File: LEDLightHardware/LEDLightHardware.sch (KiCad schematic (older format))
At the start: 1 part

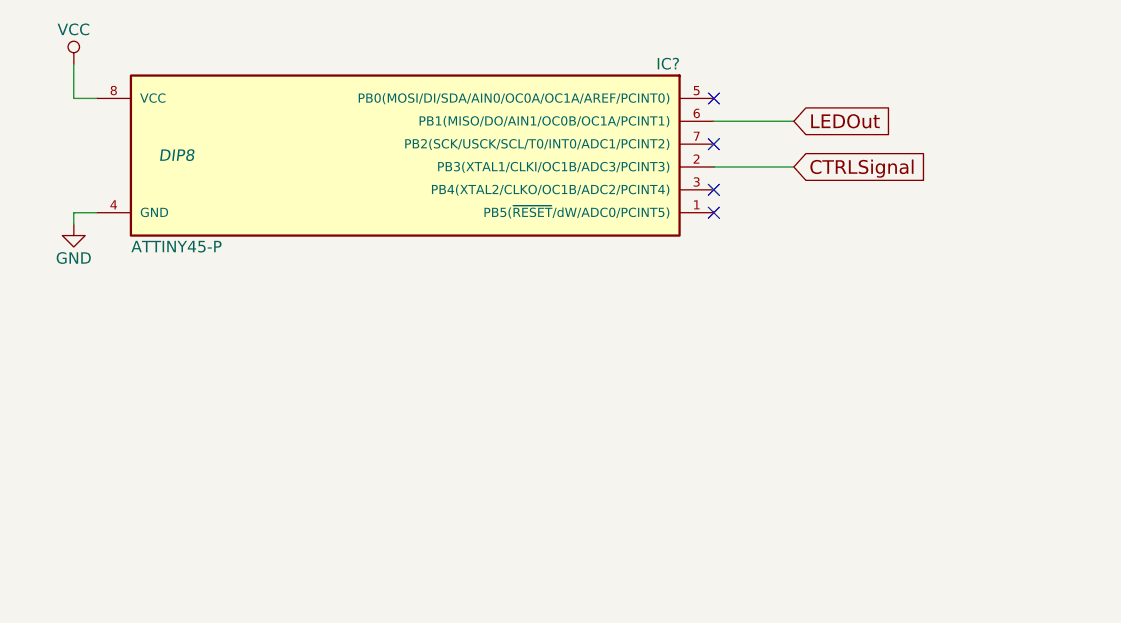
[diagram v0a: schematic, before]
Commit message: Added power input and regulation
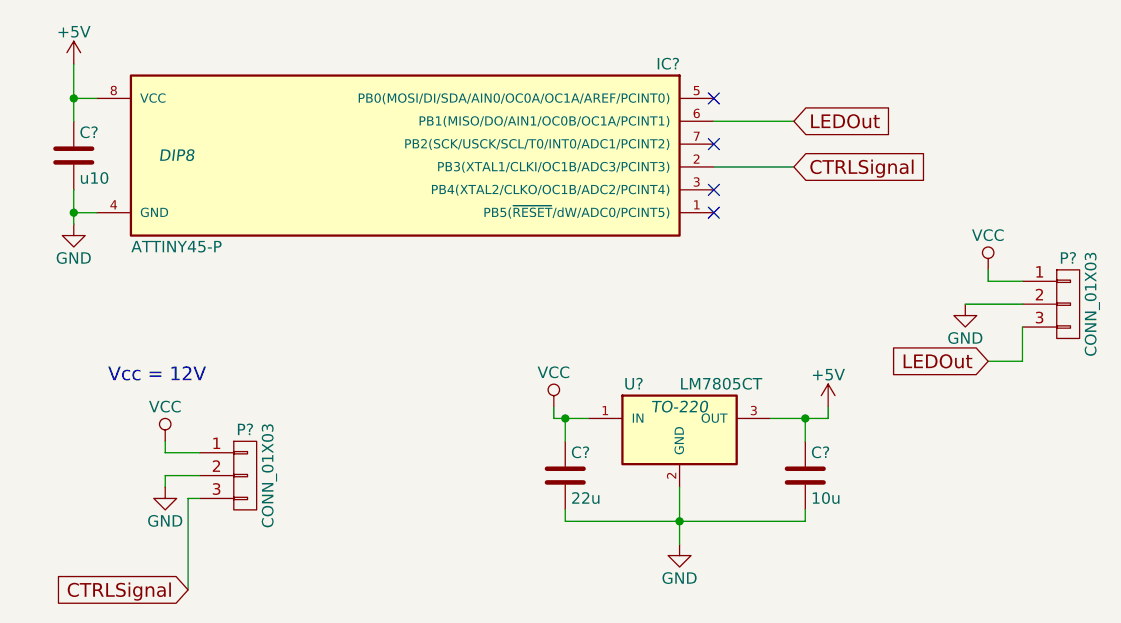
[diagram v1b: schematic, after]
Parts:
- added C?: u10, symbol C
- added C?: 22u, symbol C
- added C?: 10u, symbol C
- added P? (x2): CONN_01X03, symbol CONN_01X03
- added U?: LM7805CT, TO-220, symbol LM7805CT
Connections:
- net CTRLSignal: now also P?.3 (P3)
- net GND: now also C?.2, C?.2, C?.2, P?.2 (P2), P?.2 (P2), U?.2 (GND)
- net LEDOut: now also P?.3 (P3)
- net VCC: now also C?.1, P?.1 (P1), P?.1 (P1), U?.1 (IN); no longer IC?.8 (VCC)
- new net +5V: C?.1, C?.1, IC?.8 (VCC), U?.3 (OUT)
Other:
- note added: "Vcc = 12V"
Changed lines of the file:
@@
 	-1   0    0    -1
 $EndComp
-$Comp
-L VCC #PWR?
-U 1 1 56FFFF56
-P 1250 1050
-F 0 "#PWR?" H 1250 900 50  0001 C CNN
-F 1 "VCC" H 1250 1200 50  0000 C CNN
-F 2 "" H 1250 1050 50  0000 C CNN
-F 3 "" H 1250 1050 50  0000 C CNN
-	1    1250 1050
-	1    0    0    -1
-$EndComp
-Wire Wire Line
-	1250 1050 1250 1200
+Wire Wire Line
+	1250 1050 1250 1300
 Wire Wire Line
 	1250 1200 1350 1200
@@
 $EndComp
 Wire Wire Line
-	1250 1750 1250 1700
+	1250 1600 1250 1750
 Wire Wire Line
 	1250 1700 1350 1700
@@
 NoConn ~ 4050 1700
 NoConn ~ 4050 1600
+$Comp
+L VCC #PWR?
+U 1 1 57012428
+P 1650 2700
+F 0 "#PWR?" H 1650 2550 50  0001 C CNN
+F 1 "VCC" H 1650 2850 50  0000 C CNN
+F 2 "" H 1650 2700 50  0000 C CNN
+F 3 "" H 1650 2700 50  0000 C CNN
+	1    1650 2700
+	1    0    0    -1
+$EndComp
+Wire Wire Line
+	1650 2700 1650 2750
+Wire Wire Line
+	1650 2750 1800 2750
+$Comp
+L GND #PWR?
+U 1 1 5701244A
+P 1650 2900
+F 0 "#PWR?" H 1650 2650 50  0001 C CNN
+F 1 "GND" H 1650 2750 50  0000 C CNN
+F 2 "" H 1650 2900 50  0000 C CNN
+F 3 "" H 1650 2900 50  0000 C CNN
+	1    1650 2900
+	1    0    0    -1
+$EndComp
+Wire Wire Line
+	1650 2900 1650 2850
+Wire Wire Line
+	1650 2850 1800 2850
+$Comp
+L C C?
+U 1 1 570124BC
+P 1250 1450
+F 0 "C?" H 1275 1550 50  0000 L CNN
+F 1 "u10" H 1275 1350 50  0000 L CNN
+F 2 "" H 1288 1300 50  0000 C CNN
+F 3 "" H 1250 1450 50  0000 C CNN
+	1    1250 1450
+	1    0    0    -1
+$EndComp
+Connection ~ 1250 1200
+Connection ~ 1250 1700
+Text Notes 1400 2450 0    60   ~ 0
+Vcc = 12V
+$Comp
+L LM7805CT U?
+U 1 1 57012653
+P 3900 2650
+F 0 "U?" H 3700 2850 50  0000 C CNN
+F 1 "LM7805CT" H 3900 2850 50  0000 L CNN
+F 2 "TO-220" H 3900 2750 50  0000 C CIN
+F 3 "" H 3900 2650 50  0000 C CNN
+	1    3900 2650
+	1    0    0    -1
+$EndComp
+$Comp
+L VCC #PWR?
+U 1 1 570126D6
+P 3350 2550
+F 0 "#PWR?" H 3350 2400 50  0001 C CNN
+F 1 "VCC" H 3350 2700 50  0000 C CNN
+F 2 "" H 3350 2550 50  0000 C CNN
+F 3 "" H 3350 2550 50  0000 C CNN
+	1    3350 2550
+	1    0    0    -1
+$EndComp
+Wire Wire Line
+	3350 2550 3350 2600
+Wire Wire Line
+	3350 2600 3500 2600
+Wire Wire Line
+	3900 2900 3900 3150
+$Comp
+L +5V #PWR?
+U 1 1 57012788
+P 4550 2550
+F 0 "#PWR?" H 4550 2400 50  0001 C CNN
+F 1 "+5V" H 4550 2690 50  0000 C CNN
+F 2 "" H 4550 2550 50  0000 C CNN
+F 3 "" H 4550 2550 50  0000 C CNN
+	1    4550 2550
+	1    0    0    -1
+$EndComp
+Wire Wire Line
+	4550 2550 4550 2600
+Wire Wire Line
+	4550 2600 4300 2600
+$Comp
+L +5V #PWR?
+U 1 1 5701281E
+P 1250 1050
+F 0 "#PWR?" H 1250 900 50  0001 C CNN
+F 1 "+5V" H 1250 1190 50  0000 C CNN
+F 2 "" H 1250 1050 50  0000 C CNN
+F 3 "" H 1250 1050 50  0000 C CNN
+	1    1250 1050
+	1    0    0    -1
+$EndComp
+$Comp
+L C C?
+U 1 1 570129AF
+P 3400 2850
+F 0 "C?" H 3425 2950 50  0000 L CNN
+F 1 "22u" H 3425 2750 50  0000 L CNN
+F 2 "" H 3438 2700 50  0000 C CNN
+F 3 "" H 3400 2850 50  0000 C CNN
+	1    3400 2850
+	1    0    0    -1
+$EndComp
+Wire Wire Line
+	3400 3000 3400 3050
+Wire Wire Line
+	3400 3050 4450 3050
+$Comp
+L GND #PWR?
+U 1 1 57012A19
+P 3900 3150
+F 0 "#PWR?" H 3900 2900 50  0001 C CNN
+F 1 "GND" H 3900 3000 50  0000 C CNN
+F 2 "" H 3900 3150 50  0000 C CNN
+F 3 "" H 3900 3150 50  0000 C CNN
+	1    3900 3150
+	1    0    0    -1
+$EndComp
+Connection ~ 3900 3050
+$Comp
+L C C?
+U 1 1 57012A54
+P 4450 2850
+F 0 "C?" H 4475 2950 50  0000 L CNN
+F 1 "10u" H 4475 2750 50  0000 L CNN
+F 2 "" H 4488 2700 50  0000 C CNN
+F 3 "" H 4450 2850 50  0000 C CNN
+	1    4450 2850
+	1    0    0    -1
+$EndComp
+Wire Wire Line
+	4450 3050 4450 3000
+Wire Wire Line
+	4450 2700 4450 2600
+Connection ~ 4450 2600
+Wire Wire Line
+	3400 2700 3400 2600
+Connection ~ 3400 2600
+$Comp
+L CONN_01X03 P?
+U 1 1 57012C0D
+P 5600 2100
+F 0 "P?" H 5600 2300 50  0000 C CNN
+F 1 "CONN_01X03" V 5700 2100 50  0000 C CNN
+F 2 "" H 5600 2100 50  0000 C CNN
+F 3 "" H 5600 2100 50  0000 C CNN
+	1    5600 2100
+	1    0    0    -1
+$EndComp
+$Comp
+L VCC #PWR?
+U 1 1 57012CFB
+P 5250 1950
+F 0 "#PWR?" H 5250 1800 50  0001 C CNN
+F 1 "VCC" H 5250 2100 50  0000 C CNN
+F 2 "" H 5250 1950 50  0000 C CNN
+F 3 "" H 5250 1950 50  0000 C CNN
+	1    5250 1950
+	1    0    0    -1
+$EndComp
+Wire Wire Line
+	5250 1950 5250 2000
+Wire Wire Line
+	5250 2000 5400 2000
+$Comp
+L GND #PWR?
+U 1 1 57012D3F
+P 5150 2100
+F 0 "#PWR?" H 5150 1850 50  0001 C CNN
+F 1 "GND" H 5150 1950 50  0000 C CNN
+F 2 "" H 5150 2100 50  0000 C CNN
+F 3 "" H 5150 2100 50  0000 C CNN
+	1    5150 2100
+	1    0    0    -1
+$EndComp
+Wire Wire Line
+	5150 2100 5400 2100
+Text GLabel 5250 2350 0    60   Input ~ 0
+LEDOut
+Wire Wire Line
+	5250 2350 5400 2350
+Wire Wire Line
+	5400 2350 5400 2200
+$Comp
+L CONN_01X03 P?
+U 1 1 5701301E
+P 2000 2850
+F 0 "P?" H 2000 3050 50  0000 C CNN
+F 1 "CONN_01X03" V 2100 2850 50  0000 C CNN
+F 2 "" H 2000 2850 50  0000 C CNN
+F 3 "" H 2000 2850 50  0000 C CNN
+	1    2000 2850
+	1    0    0    -1
+$EndComp
+Text GLabel 1750 3350 0    60   Input ~ 0
+CTRLSignal
+Wire Wire Line
+	1750 3350 1750 2950
+Wire Wire Line
+	1750 2950 1800 2950
 $EndSCHEMATC

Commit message: fixed pdf schematic
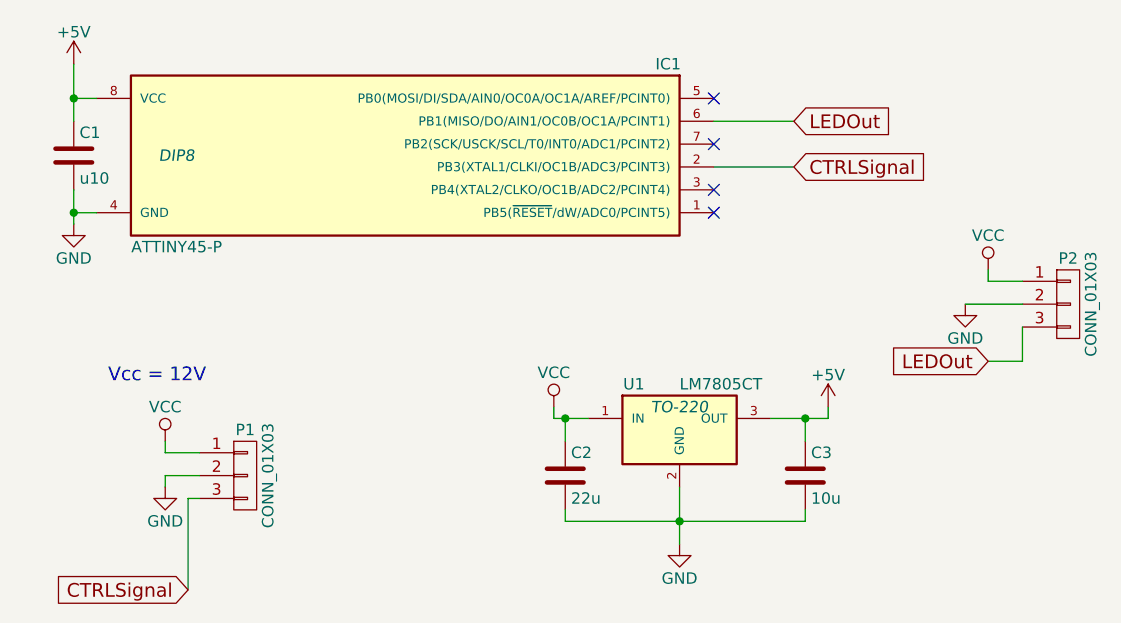
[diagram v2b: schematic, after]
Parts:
- gave numbers to parts that had none: 7
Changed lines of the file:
@@
 $EndDescr
 $Comp
-L ATTINY45-P IC?
+L ATTINY45-P IC1
 U 1 1 56FFFE4D
 P 2700 1450
-F 0 "IC?" H 1550 1850 50  0000 C CNN
+F 0 "IC1" H 1550 1850 50  0000 C CNN
 F 1 "ATTINY45-P" H 3700 1050 50  0000 C CNN
 F 2 "DIP8" H 3700 1450 50  0000 C CIN
@@
 	1250 1200 1350 1200
 $Comp
-L GND #PWR?
+L GND #PWR2
 U 1 1 56FFFF6F
 P 1250 1750
-F 0 "#PWR?" H 1250 1500 50  0001 C CNN
+F 0 "#PWR2" H 1250 1500 50  0001 C CNN
 F 1 "GND" H 1250 1600 50  0000 C CNN
 F 2 "" H 1250 1750 50  0000 C CNN
@@
 NoConn ~ 4050 1600
 $Comp
-L VCC #PWR?
+L VCC #PWR3
 U 1 1 57012428
 P 1650 2700
-F 0 "#PWR?" H 1650 2550 50  0001 C CNN
+F 0 "#PWR3" H 1650 2550 50  0001 C CNN
 F 1 "VCC" H 1650 2850 50  0000 C CNN
 F 2 "" H 1650 2700 50  0000 C CNN
@@
 	1650 2750 1800 2750
 $Comp
-L GND #PWR?
+L GND #PWR4
 U 1 1 5701244A
 P 1650 2900
-F 0 "#PWR?" H 1650 2650 50  0001 C CNN
+F 0 "#PWR4" H 1650 2650 50  0001 C CNN
 F 1 "GND" H 1650 2750 50  0000 C CNN
 F 2 "" H 1650 2900 50  0000 C CNN
@@
 	1650 2850 1800 2850
 $Comp
-L C C?
+L C C1
 U 1 1 570124BC
 P 1250 1450
-F 0 "C?" H 1275 1550 50  0000 L CNN
+F 0 "C1" H 1275 1550 50  0000 L CNN
 F 1 "u10" H 1275 1350 50  0000 L CNN
 F 2 "" H 1288 1300 50  0000 C CNN
@@
 Vcc = 12V
 $Comp
-L LM7805CT U?
+L LM7805CT U1
 U 1 1 57012653
 P 3900 2650
-F 0 "U?" H 3700 2850 50  0000 C CNN
+F 0 "U1" H 3700 2850 50  0000 C CNN
 F 1 "LM7805CT" H 3900 2850 50  0000 L CNN
 F 2 "TO-220" H 3900 2750 50  0000 C CIN
@@
 $EndComp
 $Comp
-L VCC #PWR?
+L VCC #PWR5
 U 1 1 570126D6
 P 3350 2550
-F 0 "#PWR?" H 3350 2400 50  0001 C CNN
+F 0 "#PWR5" H 3350 2400 50  0001 C CNN
 F 1 "VCC" H 3350 2700 50  0000 C CNN
 F 2 "" H 3350 2550 50  0000 C CNN
@@
 	3900 2900 3900 3150
 $Comp
-L +5V #PWR?
+L +5V #PWR7
 U 1 1 57012788
 P 4550 2550
-F 0 "#PWR?" H 4550 2400 50  0001 C CNN
+F 0 "#PWR7" H 4550 2400 50  0001 C CNN
 F 1 "+5V" H 4550 2690 50  0000 C CNN
 F 2 "" H 4550 2550 50  0000 C CNN
@@
 	4550 2600 4300 2600
 $Comp
-L +5V #PWR?
+L +5V #PWR1
 U 1 1 5701281E
 P 1250 1050
-F 0 "#PWR?" H 1250 900 50  0001 C CNN
+F 0 "#PWR1" H 1250 900 50  0001 C CNN
 F 1 "+5V" H 1250 1190 50  0000 C CNN
 F 2 "" H 1250 1050 50  0000 C CNN
@@
 $EndComp
 $Comp
-L C C?
+L C C2
 U 1 1 570129AF
 P 3400 2850
-F 0 "C?" H 3425 2950 50  0000 L CNN
+F 0 "C2" H 3425 2950 50  0000 L CNN
 F 1 "22u" H 3425 2750 50  0000 L CNN
 F 2 "" H 3438 2700 50  0000 C CNN
@@
 	3400 3050 4450 3050
 $Comp
-L GND #PWR?
+L GND #PWR6
 U 1 1 57012A19
 P 3900 3150
-F 0 "#PWR?" H 3900 2900 50  0001 C CNN
+F 0 "#PWR6" H 3900 2900 50  0001 C CNN
 F 1 "GND" H 3900 3000 50  0000 C CNN
 F 2 "" H 3900 3150 50  0000 C CNN
@@
 Connection ~ 3900 3050
 $Comp
-L C C?
+L C C3
 U 1 1 57012A54
 P 4450 2850
-F 0 "C?" H 4475 2950 50  0000 L CNN
+F 0 "C3" H 4475 2950 50  0000 L CNN
 F 1 "10u" H 4475 2750 50  0000 L CNN
 F 2 "" H 4488 2700 50  0000 C CNN
@@
 Connection ~ 3400 2600
 $Comp
-L CONN_01X03 P?
+L CONN_01X03 P2
 U 1 1 57012C0D
 P 5600 2100
-F 0 "P?" H 5600 2300 50  0000 C CNN
+F 0 "P2" H 5600 2300 50  0000 C CNN
 F 1 "CONN_01X03" V 5700 2100 50  0000 C CNN
 F 2 "" H 5600 2100 50  0000 C CNN
@@
 $EndComp
 $Comp
-L VCC #PWR?
+L VCC #PWR9
 U 1 1 57012CFB
 P 5250 1950
-F 0 "#PWR?" H 5250 1800 50  0001 C CNN
+F 0 "#PWR9" H 5250 1800 50  0001 C CNN
 F 1 "VCC" H 5250 2100 50  0000 C CNN
 F 2 "" H 5250 1950 50  0000 C CNN
@@
 	5250 2000 5400 2000
 $Comp
-L GND #PWR?
+L GND #PWR8
 U 1 1 57012D3F
 P 5150 2100
-F 0 "#PWR?" H 5150 1850 50  0001 C CNN
+F 0 "#PWR8" H 5150 1850 50  0001 C CNN
 F 1 "GND" H 5150 1950 50  0000 C CNN
 F 2 "" H 5150 2100 50  0000 C CNN
@@
 	5400 2350 5400 2200
 $Comp
-L CONN_01X03 P?
+L CONN_01X03 P1
 U 1 1 5701301E
 P 2000 2850
-F 0 "P?" H 2000 3050 50  0000 C CNN
+F 0 "P1" H 2000 3050 50  0000 C CNN
 F 1 "CONN_01X03" V 2100 2850 50  0000 C CNN
 F 2 "" H 2000 2850 50  0000 C CNN
